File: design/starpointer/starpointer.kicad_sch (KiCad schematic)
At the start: 38 parts, among them J1 2.54mm Header, J2 2.54mm Header, J3 XM7D-0512, M1 ADXL345 MODULE, M2 HMC5883L MODULE, U1 STM32F103C8T6, U2 USBLC6-2SC6, U3 RT9193-33GB, Y1 32.768kHz, Y2 8.00MHz

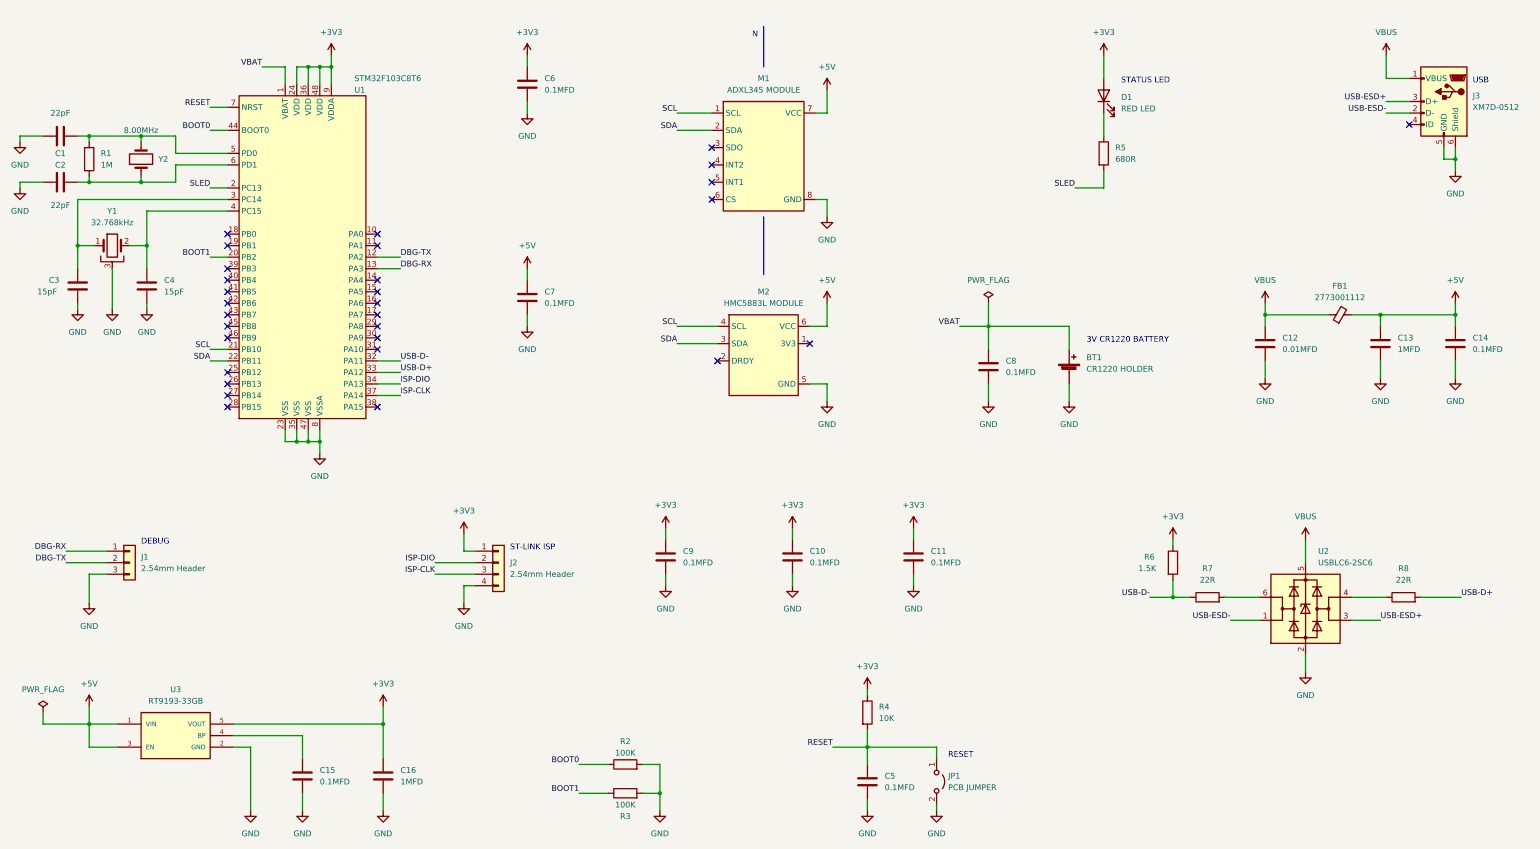
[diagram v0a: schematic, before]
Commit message: Add note about the component types. Add PDF version of the schematic.
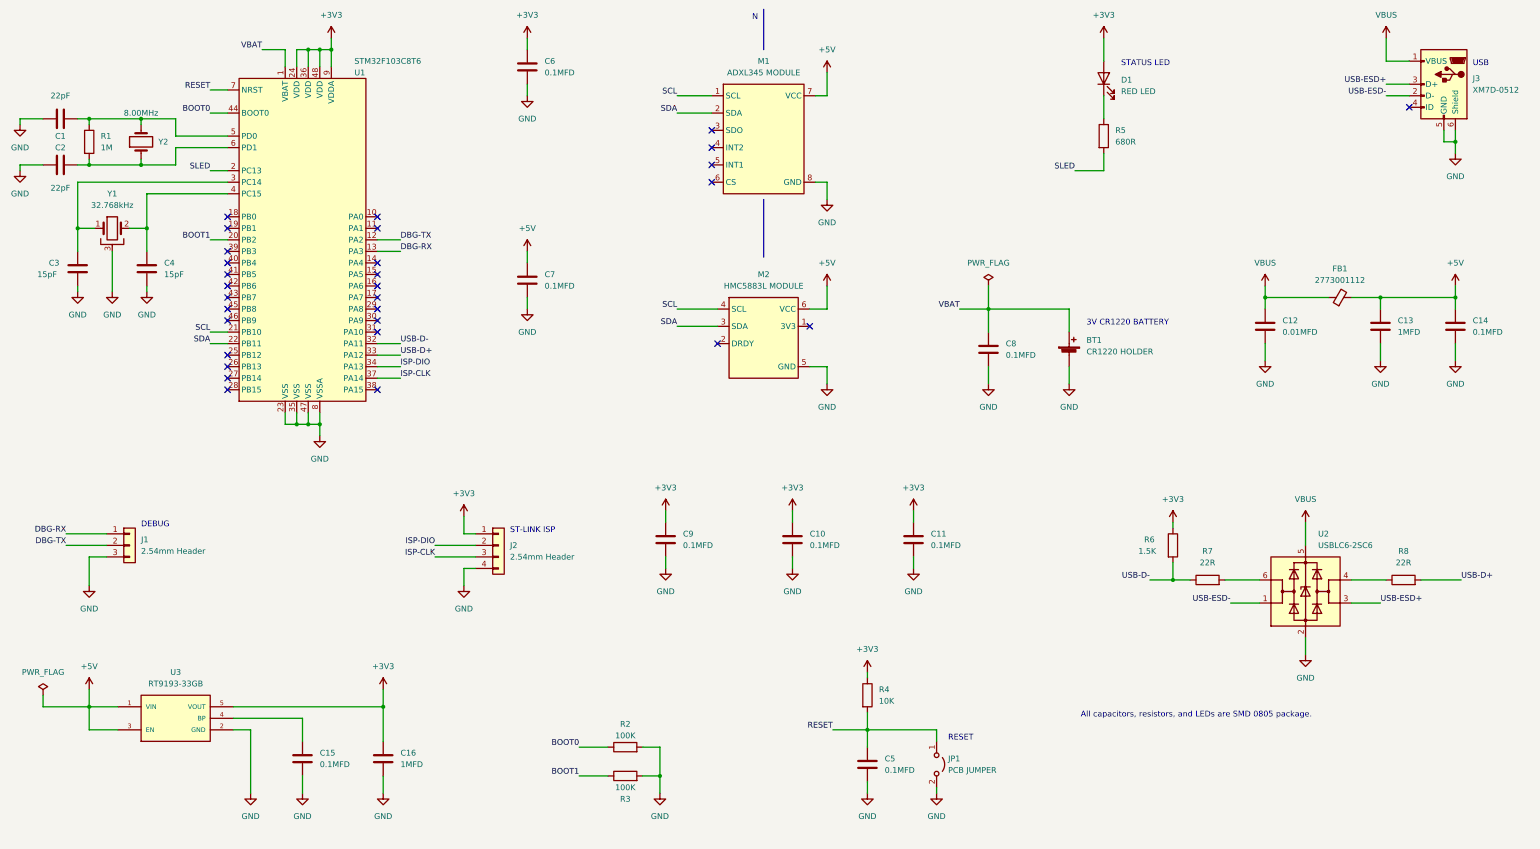
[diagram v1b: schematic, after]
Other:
- note added: "All capacitors, resistors, and LEDs are SMD 0805 package."
- moved on the sheet: BT1, C1, C10, C11, C12, C13, C14, C15, C16, C2, C3, C4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

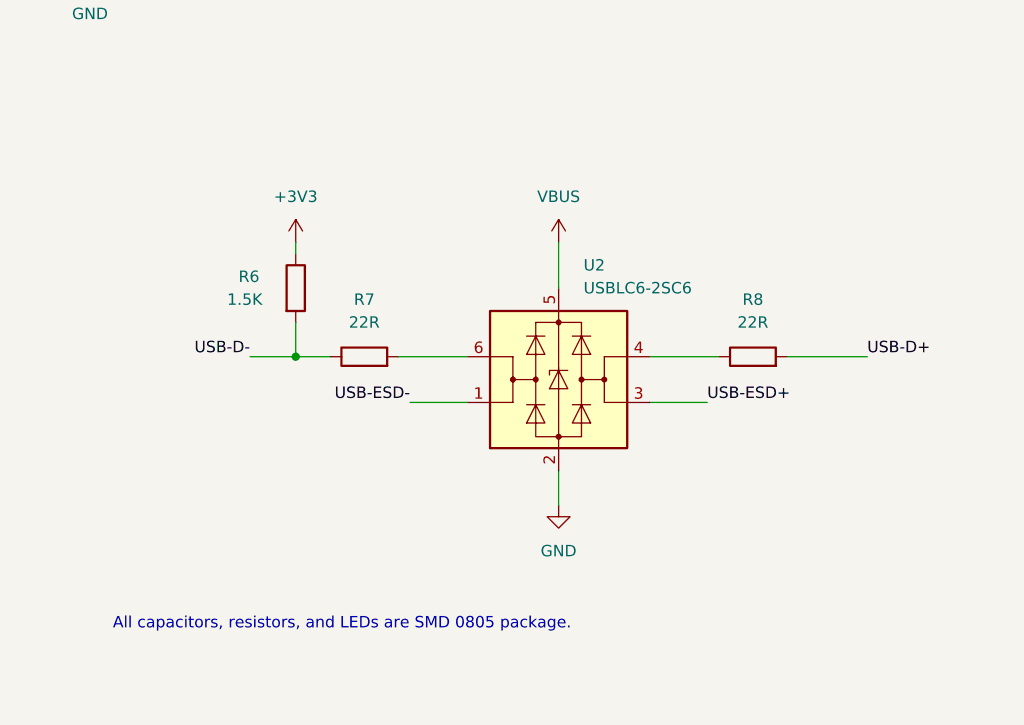
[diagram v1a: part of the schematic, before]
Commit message: Fix USB connection issue due to the missing pull-up in USB-D+ line.
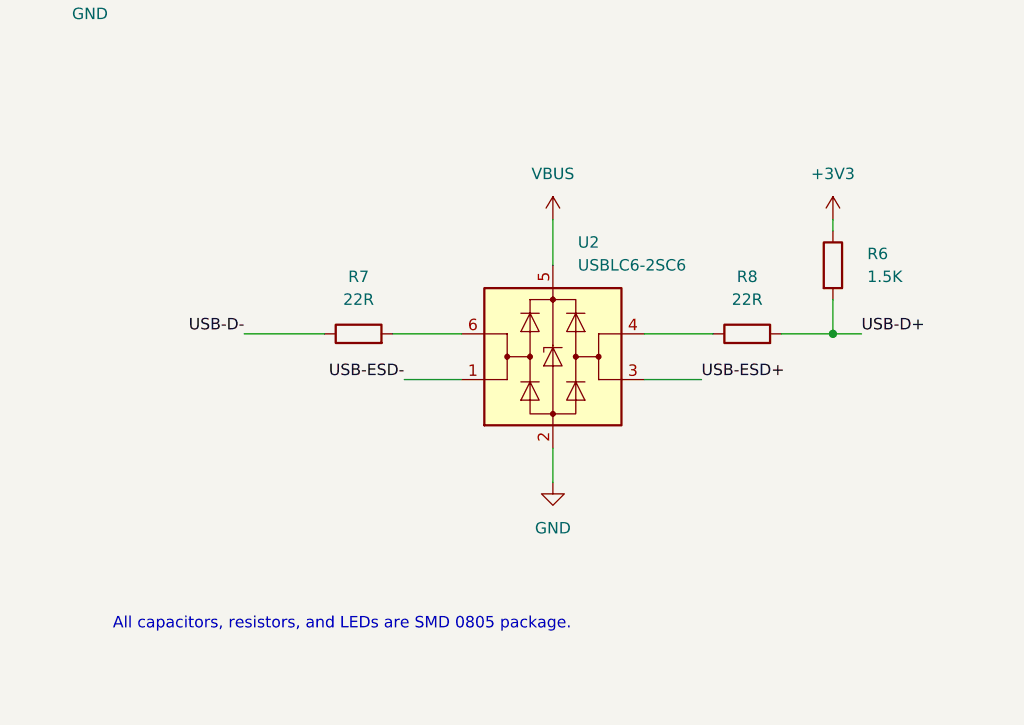
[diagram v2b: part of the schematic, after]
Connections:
- net USB-D+: now also R6.2
- net USB-D-: no longer R6.2
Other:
- moved on the sheet: R6, R7, R8, U2
